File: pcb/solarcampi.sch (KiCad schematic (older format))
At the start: 25 parts, among them J1 Conn_02x20_Odd_Even, J2 Vin 12V, J3 AVR-ISP-6, J4 FTDI, Q1 IRLML 2244, Q2 BCR 108 SMD, U1 INA226, U2 ATmega328P-AU, U3 TPS71533__SC70

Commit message: Schematic RevB
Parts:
- removed Q2: BCR 108 SMD, Package_TO_SOT_SMD:SOT-23, symbol solarcampi-rescue:DTC123J-Transistor_BJT
- removed R3: 4k7, Resistor_SMD:R_0805_2012Metric_Pad1.15x1.40mm_HandSolder, symbol Device:R
- added D1: D, Diode_SMD:D_SOD-123, symbol Device:D
- added D2: LED, LED_SMD:LED_0805_2012Metric_Pad1.15x1.40mm_HandSolder, symbol Device:LED
- added D3: D_Zener, Diode_SMD:D_SOD-123, symbol Device:D_Zener
- added F2: Fuse, Fuse:Fuse_0805_2012Metric_Pad1.15x1.40mm_HandSolder, symbol Device:Fuse
- added J3: FTDI_AVR, Connector_PinHeader_2.54mm:PinHeader_1x06_P2.54mm_Vertical, symbol Connector:Conn_01x06_Male
- added JP2, JP3, JP4, JP5: Jumper_NO_Small, Jumper:SolderJumper-2_P1.3mm_Open_Pad1.0x1.5mm, symbol Device:Jumper_NO_Small
- added Q1, Q3, Q4: Q_NMOS_GDS, Package_TO_SOT_SMD:SOT-23, symbol Device:Q_NMOS_GDS
- added R2: R, Resistor_SMD:R_0805_2012Metric_Pad1.15x1.40mm_HandSolder, symbol Device:R
- added R4: 4k7, Resistor_SMD:R_0805_2012Metric_Pad1.15x1.40mm_HandSolder, symbol Device:R
- added R6, R7, R8: 1M, Resistor_SMD:R_0805_2012Metric_Pad1.15x1.40mm_HandSolder, symbol Device:R
- added TP1: 12V, TestPoint:TestPoint_Pad_1.0x1.0mm, symbol Connector:TestPoint
- added TP2: 3V3, TestPoint:TestPoint_Pad_1.0x1.0mm, symbol Connector:TestPoint
- added TP3: 5V, TestPoint:TestPoint_Pad_1.0x1.0mm, symbol Connector:TestPoint
- J5: renamed from J4; value FTDI -> FTDI_RPI
- R5: renamed from R1; value 10k -> 1M
- renumbered C5 to C1, C3 to C2, C1 to C3, C7 to C5, C9 to C6, C2 to C7, C6 to C8, C8 to C9, J2 to J1, J3 to J2, J1 to J4, Q1 to Q2, R2 to R1, R4 to R3, U3 to U2, U2 to U3
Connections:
- net labels added: PWR_OVR, RST, RXD, TXD
- wire segments 52 -> 118
- no-connect marks 39 -> 36
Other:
- moved on the sheet: C5, C7, R3

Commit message: Layout RevB
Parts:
- removed JP1: Jumper_2_Open, Jumper:SolderJumper-2_P1.3mm_Open_Pad1.0x1.5mm, symbol Jumper:Jumper_2_Open
- C6: value 100n -> C
- JP2: footprint Jumper:SolderJumper-2_P1.3mm_Open_Pad1.0x1.5mm -> Connector_PinHeader_2.54mm:PinHeader_1x02_P2.54mm_Vertical
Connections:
- net labels removed: AVR_I2C_PULLUP
- wire segments 118 -> 119
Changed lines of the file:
@@
-$EndComp
-$Comp
-L Jumper:Jumper_2_Open JP1
-U 1 1 5CFC428F
-P 5700 700
-F 0 "JP1" H 5700 935 50  0000 C CNN
-F 1 "Jumper_2_Open" H 5700 844 50  0000 C CNN
-F 2 "Jumper:SolderJumper-2_P1.3mm_Open_Pad1.0x1.5mm" H 5700 700 50  0001 C CNN
-F 3 "~" H 5700 700 50  0001 C CNN
-	1    5700 700
-	1    0    0    -1
 $EndComp
 $Comp
@@
 	-1   0    0    -1
 $EndComp
-Wire Wire Line
-	5050 700  5500 700
-Connection ~ 5050 700
 Text Label 5250 1300 0    50   ~ 0
 ~RST
@@
 	1    0    0    -1
 $EndComp
-$Comp
-L Device:C C6
-U 1 1 5D17957D
-P 2700 2650
-F 0 "C6" H 2815 2696 50  0000 L CNN
-F 1 "100n" H 2815 2605 50  0000 L CNN
-F 2 "Capacitor_SMD:C_0805_2012Metric_Pad1.15x1.40mm_HandSolder" H 2738 2500 50  0001 C CNN
-F 3 "~" H 2700 2650 50  0001 C CNN
-	1    2700 2650
-	1    0    0    -1
-$EndComp
-Text Label 2700 2500 0    50   ~ 0
-AVR_I2C_PULLUP
-$Comp
-L power:GND #PWR011
-U 1 1 5D17E891
-P 2700 2800
-F 0 "#PWR011" H 2700 2550 50  0001 C CNN
-F 1 "GND" H 2705 2627 50  0000 C CNN
-F 2 "" H 2700 2800 50  0001 C CNN
-F 3 "" H 2700 2800 50  0001 C CNN
-	1    2700 2800
-	1    0    0    -1
-$EndComp
 Text Label 5600 3500 0    50   ~ 0
 AVR_PWR_EN
@@
 Connection ~ 5400 2550
 $Comp
-L Device:Jumper_NO_Small JP2
-U 1 1 5D102195
-P 6150 2450
-F 0 "JP2" H 6150 2635 50  0000 C CNN
-F 1 "Jumper_NO_Small" H 6150 2544 50  0000 C CNN
-F 2 "Jumper:SolderJumper-2_P1.3mm_Open_Pad1.0x1.5mm" H 6150 2450 50  0001 C CNN
-F 3 "~" H 6150 2450 50  0001 C CNN
-	1    6150 2450
-	1    0    0    -1
-$EndComp
-$Comp
 L power:GND #PWR017
 U 1 1 5D102B31
@@
 Wire Wire Line
 	5050 3950 4050 3950
+$Comp
+L Device:C C6
+U 1 1 5D19A2A4
+P 6850 1250
+F 0 "C6" H 6735 1204 50  0000 R CNN
+F 1 "C" H 6735 1295 50  0000 R CNN
+F 2 "Capacitor_SMD:C_0805_2012Metric_Pad1.15x1.40mm_HandSolder" H 6888 1100 50  0001 C CNN
+F 3 "~" H 6850 1250 50  0001 C CNN
+	1    6850 1250
+	-1   0    0    1
+$EndComp
+$Comp
+L power:+12V #PWR0101
+U 1 1 5D19B372
+P 6850 1000
+F 0 "#PWR0101" H 6850 850 50  0001 C CNN
+F 1 "+12V" H 6865 1173 50  0000 C CNN
+F 2 "" H 6850 1000 50  0001 C CNN
+F 3 "" H 6850 1000 50  0001 C CNN
+	1    6850 1000
+	1    0    0    -1
+$EndComp
+Wire Wire Line
+	6850 1000 6850 1100
+$Comp
+L power:GND #PWR0102
+U 1 1 5D19FFB1
+P 6850 1500
+F 0 "#PWR0102" H 6850 1250 50  0001 C CNN
+F 1 "GND" H 6855 1327 50  0000 C CNN
+F 2 "" H 6850 1500 50  0001 C CNN
+F 3 "" H 6850 1500 50  0001 C CNN
+	1    6850 1500
+	1    0    0    -1
+$EndComp
+Wire Wire Line
+	6850 1500 6850 1400
+$Comp
+L Device:Jumper_NO_Small JP2
+U 1 1 5D102195
+P 6150 2450
+F 0 "JP2" H 6150 2635 50  0000 C CNN
+F 1 "Jumper_NO_Small" H 6150 2544 50  0000 C CNN
+F 2 "Connector_PinHeader_2.54mm:PinHeader_1x02_P2.54mm_Vertical" H 6150 2450 50  0001 C CNN
+F 3 "~" H 6150 2450 50  0001 C CNN
+	1    6150 2450
+	1    0    0    -1
+$EndComp
 $EndSCHEMATC

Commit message: Add more GND pins to reduce GND loop area
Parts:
- J1: footprint TerminalBlock:TerminalBlock_bornier-2_P5.08mm -> solarcampi:TerminalBlock_bornier-2_P5.08mm
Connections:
- no-connect marks 36 -> 35
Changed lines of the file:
@@
 F 0 "J1" H 1280 1042 50  0000 L CNN
 F 1 "Vin 12V" H 1280 951 50  0000 L CNN
-F 2 "TerminalBlock:TerminalBlock_bornier-2_P5.08mm" H 1200 1050 50  0001 C CNN
+F 2 "solarcampi:TerminalBlock_bornier-2_P5.08mm" H 1200 1050 50  0001 C CNN
 F 3 "~" H 1200 1050 50  0001 C CNN
 	1    1200 1050
@@
 NoConn ~ 10100 3300
 NoConn ~ 10100 3400
-NoConn ~ 9600 2400
 NoConn ~ 9600 2700
 NoConn ~ 9600 2800
@@
 	1    0    0    -1
 $EndComp
+$Comp
+L power:GND #PWR0103
+U 1 1 5D21EF2D
+P 9600 2400
+F 0 "#PWR0103" H 9600 2150 50  0001 C CNN
+F 1 "GND" V 9605 2272 50  0000 R CNN
+F 2 "" H 9600 2400 50  0001 C CNN
+F 3 "" H 9600 2400 50  0001 C CNN
+	1    9600 2400
+	0    1    1    0
+$EndComp
 $EndSCHEMATC

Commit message: Fix RevB errata
- Fix SOT23 NMOS pinout
- Fix AVR reset circuitry
- Add ceramic snubber to suppress ringing at input
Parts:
- removed Q1, Q3, Q4: Q_NMOS_GDS, Package_TO_SOT_SMD:SOT-23, symbol Device:Q_NMOS_GDS
- added C10: 100u, Capacitor_SMD:C_1210_3225Metric_Pad1.42x2.65mm_HandSolder, symbol Device:C
- added C11: 100n, Capacitor_SMD:C_0805_2012Metric_Pad1.15x1.40mm_HandSolder, symbol Device:C
- added Q1, Q3, Q4: Q_NMOS_GSD, Package_TO_SOT_SMD:SOT-23, symbol Device:Q_NMOS_GSD
- added R10: 1k, Resistor_SMD:R_0805_2012Metric_Pad1.15x1.40mm_HandSolder, symbol Device:R
- added R9: 0.5R, Resistor_SMD:R_1210_3225Metric_Pad1.42x2.65mm_HandSolder, symbol Device:R
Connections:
- wire segments 119 -> 126
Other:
- moved on the sheet: C3, D1, F1, J1, J3, JP2, R5, R6, R7

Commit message: Add current shunt
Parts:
- added C12: C, Capacitor_SMD:C_0805_2012Metric_Pad1.15x1.40mm_HandSolder, symbol Device:C
- added J6: Shunt, solarcampi:TerminalBlock_bornier-2_P5.08mm, symbol solarcampi-rescue:Screw_Terminal_01x02-Connector
- added R11: R, Resistor_SMD:R_1210_3225Metric_Pad1.42x2.65mm_HandSolder, symbol Device:R
- JP3, JP4, JP5: footprint Jumper:SolderJumper-2_P1.3mm_Open_Pad1.0x1.5mm -> Jumper:SolderJumper-2_P1.3mm_Bridged_Pad1.0x1.5mm; symbol Device:Jumper_NO_Small -> Device:Jumper_NC_Small
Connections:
- net SHUNT+: now reaches U1.10 (Vin+)
- net SHUNT+: now also C12.1, J6.1 (Pin_1), R11.1
- net SHUNT-: now reaches U1.9 (Vin-)
- net SHUNT-: now also C12.2, J6.2 (Pin_2), R11.2
- no-connect marks 35 -> 33
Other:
- moved on the sheet: C1, U1
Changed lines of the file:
@@
 L solarcampi-rescue:+12V-power #PWR03
 U 1 1 5CEFAE76
-P 1150 3600
-F 0 "#PWR03" H 1150 3450 50  0001 C CNN
-F 1 "+12V" H 1165 3773 50  0000 C CNN
-F 2 "" H 1150 3600 50  0001 C CNN
-F 3 "" H 1150 3600 50  0001 C CNN
-	1    1150 3600
+P 2000 3950
+F 0 "#PWR03" H 2000 3800 50  0001 C CNN
+F 1 "+12V" H 2015 4123 50  0000 C CNN
+F 2 "" H 2000 3950 50  0001 C CNN
+F 3 "" H 2000 3950 50  0001 C CNN
+	1    2000 3950
 	1    0    0    -1
 $EndComp
@@
 L solarcampi-rescue:GND-power #PWR04
 U 1 1 5CEFB5C4
-P 1550 4400
-F 0 "#PWR04" H 1550 4150 50  0001 C CNN
-F 1 "GND" H 1555 4227 50  0000 C CNN
-F 2 "" H 1550 4400 50  0001 C CNN
-F 3 "" H 1550 4400 50  0001 C CNN
-	1    1550 4400
+P 2400 4950
+F 0 "#PWR04" H 2400 4700 50  0001 C CNN
+F 1 "GND" H 2405 4777 50  0000 C CNN
+F 2 "" H 2400 4950 50  0001 C CNN
+F 3 "" H 2400 4950 50  0001 C CNN
+	1    2400 4950
 	1    0    0    -1
 $EndComp
@@
 L solarcampi-rescue:GND-power #PWR08
 U 1 1 5CEFBC6A
-P 1950 3600
-F 0 "#PWR08" H 1950 3350 50  0001 C CNN
-F 1 "GND" V 1955 3472 50  0000 R CNN
-F 2 "" H 1950 3600 50  0001 C CNN
-F 3 "" H 1950 3600 50  0001 C CNN
-	1    1950 3600
+P 2800 3950
+F 0 "#PWR08" H 2800 3700 50  0001 C CNN
+F 1 "GND" V 2805 3822 50  0000 R CNN
+F 2 "" H 2800 3950 50  0001 C CNN
+F 3 "" H 2800 3950 50  0001 C CNN
+	1    2800 3950
 	0    -1   -1   0
 $EndComp
@@
 L solarcampi-rescue:GND-power #PWR09
 U 1 1 5CEFC45E
-P 1950 3700
-F 0 "#PWR09" H 1950 3450 50  0001 C CNN
-F 1 "GND" V 1955 3572 50  0000 R CNN
-F 2 "" H 1950 3700 50  0001 C CNN
-F 3 "" H 1950 3700 50  0001 C CNN
-	1    1950 3700
+P 2800 4050
+F 0 "#PWR09" H 2800 3800 50  0001 C CNN
+F 1 "GND" V 2805 3922 50  0000 R CNN
+F 2 "" H 2800 4050 50  0001 C CNN
+F 3 "" H 2800 4050 50  0001 C CNN
+	1    2800 4050
 	0    -1   -1   0
 $EndComp
-NoConn ~ 1950 4200
+NoConn ~ 2800 4550
 $Comp
 L solarcampi-rescue:+3V3-power #PWR015
@@
 L solarcampi-rescue:C-Device C1
 U 1 1 5CF3656D
-P 650 3800
-F 0 "C1" H 765 3846 50  0000 L CNN
-F 1 "100n" H 765 3755 50  0000 L CNN
-F 2 "Capacitor_SMD:C_0805_2012Metric_Pad1.15x1.40mm_HandSolder" H 688 3650 50  0001 C CNN
-F 3 "~" H 650 3800 50  0001 C CNN
-	1    650  3800
-	1    0    0    -1
-$EndComp
-$Comp
-L solarcampi-rescue:GND-power #PWR01
-U 1 1 5CF37D1D
-P 650 3950
-F 0 "#PWR01" H 650 3700 50  0001 C CNN
-F 1 "GND" H 655 3777 50  0000 C CNN
-F 2 "" H 650 3950 50  0001 C CNN
-F 3 "" H 650 3950 50  0001 C CNN
-	1    650  3950
+P 3400 4200
+F 0 "C1" H 3515 4246 50  0000 L CNN
+F 1 "100n" H 3515 4155 50  0000 L CNN
+F 2 "Capacitor_SMD:C_0805_2012Metric_Pad1.15x1.40mm_HandSolder" H 3438 4050 50  0001 C CNN
+F 3 "~" H 3400 4200 50  0001 C CNN
+	1    3400 4200
 	1    0    0    -1
 $EndComp
@@
 Wire Wire Line
 	1150 950  1150 1150
-$Comp
-L solarcampi-rescue:INA226-Analog_ADC U1
-U 1 1 5CEC0CDE
-P 1550 3900
-F 0 "U1" H 1550 4581 50  0000 C CNN
-F 1 "INA226" H 1550 4490 50  0000 C CNN
-F 2 "Package_SO:MSOP-10_3x3mm_P0.5mm" H 1600 4000 50  0001 C CNN
-F 3 "http://www.ti.com/lit/ds/symlink/ina226.pdf" H 1900 3800 50  0001 C CNN
-	1    1550 3900
-	1    0    0    -1
-$EndComp
-NoConn ~ 1150 4000
-NoConn ~ 1150 4100
 NoConn ~ 9600 2000
 NoConn ~ 10100 2100
@@
 Text Label 5000 2000 2    50   ~ 0
 AVR_SDA
-Text Label 1950 3900 0    50   ~ 0
+Text Label 2800 4250 0    50   ~ 0
 AVR_SDA
-Text Label 1950 4000 0    50   ~ 0
+Text Label 2800 4350 0    50   ~ 0
 AVR_SCL
 $Comp
@@
 	1    0    0    -1
 $EndComp
-Text Label 1550 3400 0    50   ~ 0
-INA_3V3
-Text Label 650  3650 0    50   ~ 0
+Text Label 2400 3650 0    50   ~ 0
 INA_3V3
 Text Label 5000 2100 2    50   ~ 0
@@
 	9200 3300 9000 3300
 $Comp
-L Device:Jumper_NO_Small JP3
+L Device:Jumper_NC_Small JP3
 U 1 1 5D09AB3F
 P 8900 2700
 F 0 "JP3" H 8900 2885 50  0000 C CNN
 F 1 "Jumper_NO_Small" H 8900 2794 50  0000 C CNN
-F 2 "Jumper:SolderJumper-2_P1.3mm_Open_Pad1.0x1.5mm" H 8900 2700 50  0001 C CNN
+F 2 "Jumper:SolderJumper-2_P1.3mm_Bridged_Pad1.0x1.5mm" H 8900 2700 50  0001 C CNN
 F 3 "~" H 8900 2700 50  0001 C CNN
 	1    8900 2700
@@
 $EndComp
 $Comp
-L Device:Jumper_NO_Small JP4
+L Device:Jumper_NC_Small JP4
 U 1 1 5D09B0DF
 P 8900 3000
 F 0 "JP4" H 8900 3185 50  0000 C CNN
 F 1 "Jumper_NO_Small" H 8900 3094 50  0000 C CNN
-F 2 "Jumper:SolderJumper-2_P1.3mm_Open_Pad1.0x1.5mm" H 8900 3000 50  0001 C CNN
+F 2 "Jumper:SolderJumper-2_P1.3mm_Bridged_Pad1.0x1.5mm" H 8900 3000 50  0001 C CNN
 F 3 "~" H 8900 3000 50  0001 C CNN
 	1    8900 3000
@@
 $EndComp
 $Comp
-L Device:Jumper_NO_Small JP5
+L Device:Jumper_NC_Small JP5
 U 1 1 5D09C8F7
 P 8900 3300
 F 0 "JP5" H 8900 3485 50  0000 C CNN
 F 1 "Jumper_NO_Small" H 8900 3394 50  0000 C CNN
-F 2 "Jumper:SolderJumper-2_P1.3mm_Open_Pad1.0x1.5mm" H 8900 3300 50  0001 C CNN
+F 2 "Jumper:SolderJumper-2_P1.3mm_Bridged_Pad1.0x1.5mm" H 8900 3300 50  0001 C CNN
 F 3 "~" H 8900 3300 50  0001 C CNN
 	1    8900 3300
@@
 Wire Wire Line
 	9650 4200 10200 4200
+$Comp
+L solarcampi-rescue:INA226-Analog_ADC U1
+U 1 1 5CEC0CDE
+P 2400 4250
+F 0 "U1" H 2200 4700 50  0000 C CNN
+F 1 "INA226" H 2600 4700 50  0000 C CNN
+F 2 "Package_SO:MSOP-10_3x3mm_P0.5mm" H 2450 4350 50  0001 C CNN
+F 3 "http://www.ti.com/lit/ds/symlink/ina226.pdf" H 2750 4150 50  0001 C CNN
+	1    2400 4250
+	1    0    0    -1
+$EndComp
+Text Label 1250 4200 0    50   ~ 0
+SHUNT+
+Text Label 1250 4600 0    50   ~ 0
+SHUNT-
+Wire Wire Line
+	2400 4950 2400 4850
+Wire Wire Line
+	2400 3750 2400 3650
+Wire Wire Line
+	2400 3650 3400 3650
+Wire Wire Line
+	3400 3650 3400 4050
+Wire Wire Line
+	3400 4350 3400 4850
+Wire Wire Line
+	3400 4850 2400 4850
+Connection ~ 2400 4850
+Wire Wire Line
+	2400 4850 2400 4750
+$Comp
+L Device:C C12
+U 1 1 5D49A050
+P 1600 4400
+F 0 "C12" H 1715 4446 50  0000 L CNN
+F 1 "C" H 1715 4355 50  0000 L CNN
+F 2 "Capacitor_SMD:C_0805_2012Metric_Pad1.15x1.40mm_HandSolder" H 1638 4250 50  0001 C CNN
+F 3 "~" H 1600 4400 50  0001 C CNN
+	1    1600 4400
+	1    0    0    -1
+$EndComp
+$Comp
+L Device:R R11
+U 1 1 5D4BFA64
+P 1250 4400
+F 0 "R11" H 1320 4446 50  0000 L CNN
+F 1 "R" H 1320 4355 50  0000 L CNN
+F 2 "Resistor_SMD:R_1210_3225Metric_Pad1.42x2.65mm_HandSolder" V 1180 4400 50  0001 C CNN
+F 3 "~" H 1250 4400 50  0001 C CNN
+	1    1250 4400
+	1    0    0    -1
+$EndComp
+Wire Wire Line
+	2000 4350 1900 4350
+Wire Wire Line
+	1900 4350 1900 4200
+Wire Wire Line
+	2000 4450 1900 4450
+Wire Wire Line
+	1900 4450 1900 4600
+Wire Wire Line
+	1600 4250 1600 4200
+Connection ~ 1600 4200
+Wire Wire Line
+	1600 4200 1900 4200
+Wire Wire Line
+	1600 4550 1600 4600
+Connection ~ 1600 4600
+Wire Wire Line
+	1600 4600 1900 4600
+Wire Wire Line
+	1250 4250 1250 4200
+Wire Wire Line
+	1250 4200 1600 4200
+Wire Wire Line
+	1250 4550 1250 4600
+Wire Wire Line
+	1250 4600 1600 4600
+Wire Wire Line
+	1100 4350 1100 4200
+Wire Wire Line
+	1100 4200 1250 4200
+Connection ~ 1250 4200
+Wire Wire Line
+	1100 4450 1100 4600
+Wire Wire Line
+	1100 4600 1250 4600
+Connection ~ 1250 4600
+$Comp
+L solarcampi-rescue:Screw_Terminal_01x02-Connector J6
+U 1 1 5D510791
+P 900 4350
+F 0 "J6" H 980 4342 50  0000 L CNN
+F 1 "Shunt" H 980 4251 50  0000 L CNN
+F 2 "solarcampi:TerminalBlock_bornier-2_P5.08mm" H 900 4350 50  0001 C CNN
+F 3 "~" H 900 4350 50  0001 C CNN
+	1    900  4350
+	-1   0    0    -1
+$EndComp
 $EndSCHEMATC

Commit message: Update 3d models
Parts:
- PS1: value MP1584EN -> TPS63070-compat; footprint solarcampi:MP1584_buck_module -> tps63070-module:TPS63070-module-compat; symbol custom:MP1584ENBB -> tps63070-module:TPS63070-module-compat
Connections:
- net GND: now also PS1.4 (GND); no longer PS1.3 (VOUTGND)
- net RPI_5V: now also PS1.3 (VOUT); no longer PS1.4 (VOUT)
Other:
- moved on the sheet: PS1
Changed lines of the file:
@@
 Date "2019-05-27"
 Rev "A"
-Comp "Tobias Mädel (@manawyrm)"
+Comp "Tobias Mädel (@manawyrm), Tobias Schramm (@Toble_Miner)"
 Comment1 "https://tbspace.de"
 Comment2 ""
@@
 AVR_PWR_EN
 $Comp
-L custom:MP1584ENBB PS1
+L tps63070-module:TPS63070-module-compat PS1
 U 1 1 5CFCCCFD
-P 7850 2400
-F 0 "PS1" H 7850 2767 50  0000 C CNN
-F 1 "MP1584EN" H 7850 2676 50  0000 C CNN
-F 2 "solarcampi:MP1584_buck_module" H 6800 2150 50  0001 L CNN
-F 3 "" H 8900 2100 50  0001 L CNN
-	1    7850 2400
+P 8200 2150
+F 0 "PS1" H 8200 2517 50  0000 C CNN
+F 1 "TPS63070-compat" H 8200 2426 50  0000 C CNN
+F 2 "tps63070-module:TPS63070-module-compat" H 7150 1900 50  0001 L CNN
+F 3 "" H 9250 1850 50  0001 L CNN
+	1    8200 2150
 	1    0    0    -1
 $EndComp
 Text Label 7350 2050 1    50   ~ 0
 +12V_SWITCHED
-Wire Wire Line
-	7150 2050 7550 2050
 Text Label 8900 1700 0    50   ~ 0
 RPI_5V
@@
 	-1   0    0    -1
 $EndComp
+Wire Wire Line
+	7150 2050 7800 2050
+Wire Wire Line
+	7550 2250 7800 2250
+Wire Wire Line
+	8600 2050 8750 2050
+Wire Wire Line
+	8600 2250 8750 2250
 $EndSCHEMATC

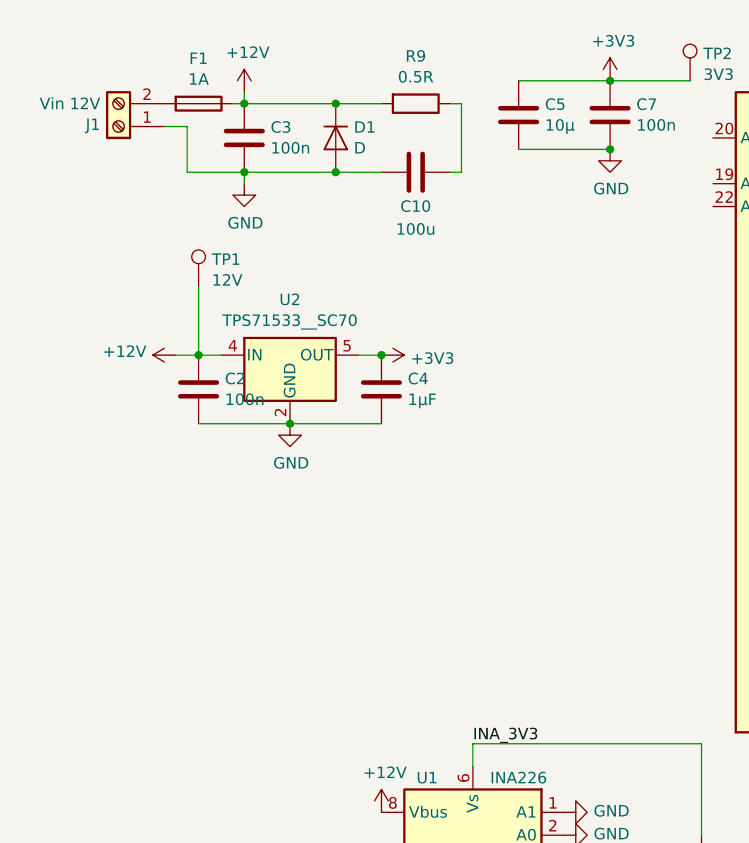
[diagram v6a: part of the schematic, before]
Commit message: Add big electrolytic cap for further suppression of ringing
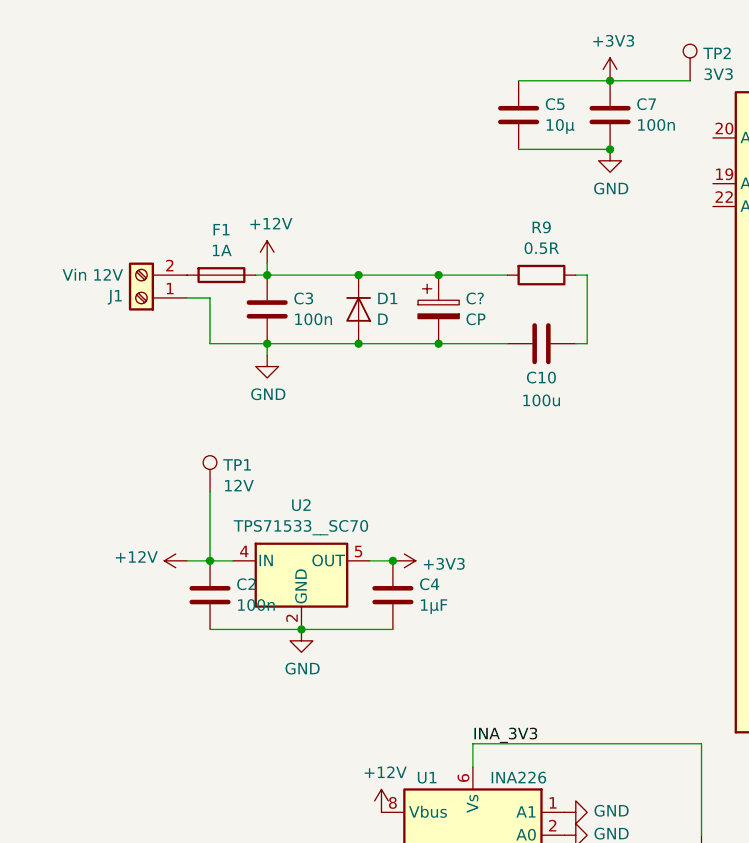
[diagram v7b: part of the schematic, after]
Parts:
- added C?: CP, Capacitor_SMD:CP_Elec_5x5.4, symbol Device:CP
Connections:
- net +12V: now also C?.1
- net GND: now also C?.2
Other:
- moved on the sheet: C10, C2, C3, C4, D1, F1, J1, R9, TP1, U2
